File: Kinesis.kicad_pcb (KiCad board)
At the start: 2 copper layers, 122 x 86 mm, 16 parts, among them J1 Right Function, J2 Right Main, J3 Right Thumb, J4 Left Thumb, J5 Left Main, J6 Left Function, U1 proton_c

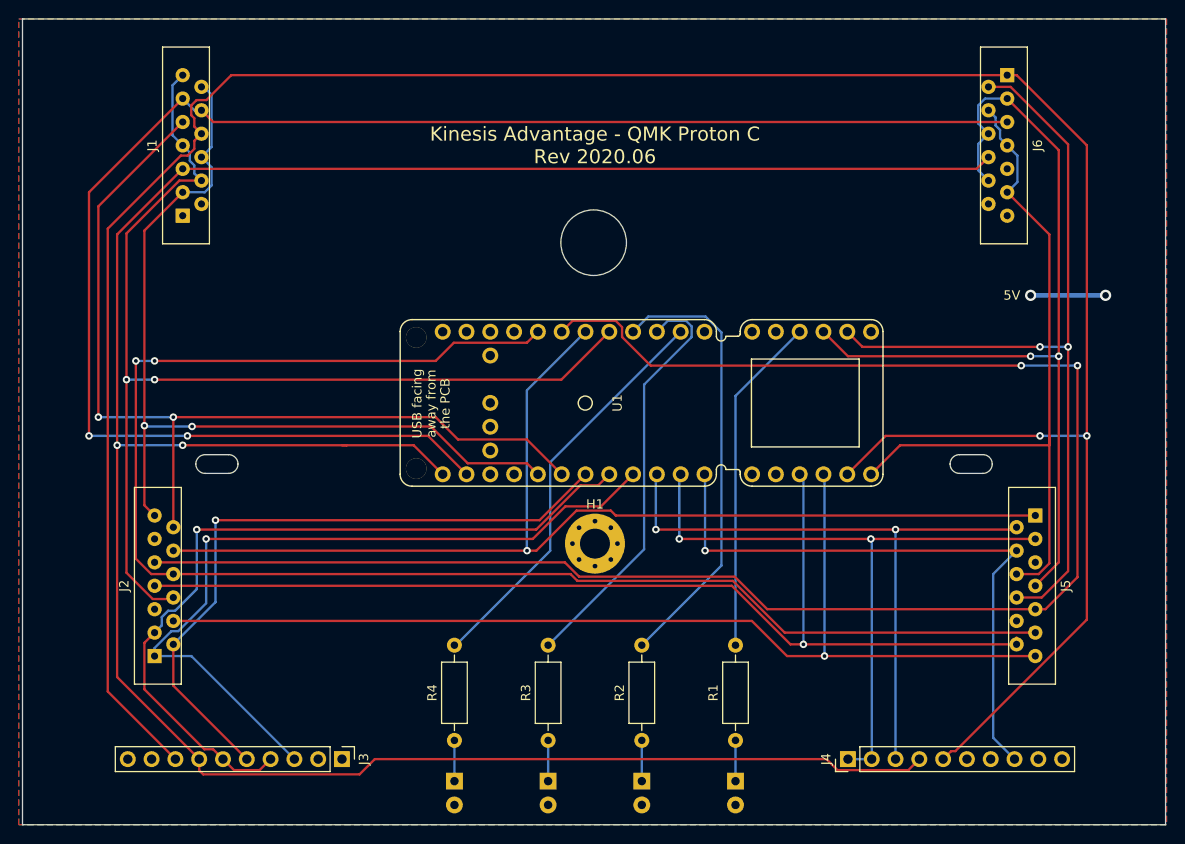
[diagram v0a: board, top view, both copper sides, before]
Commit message: Fix Molex footprints
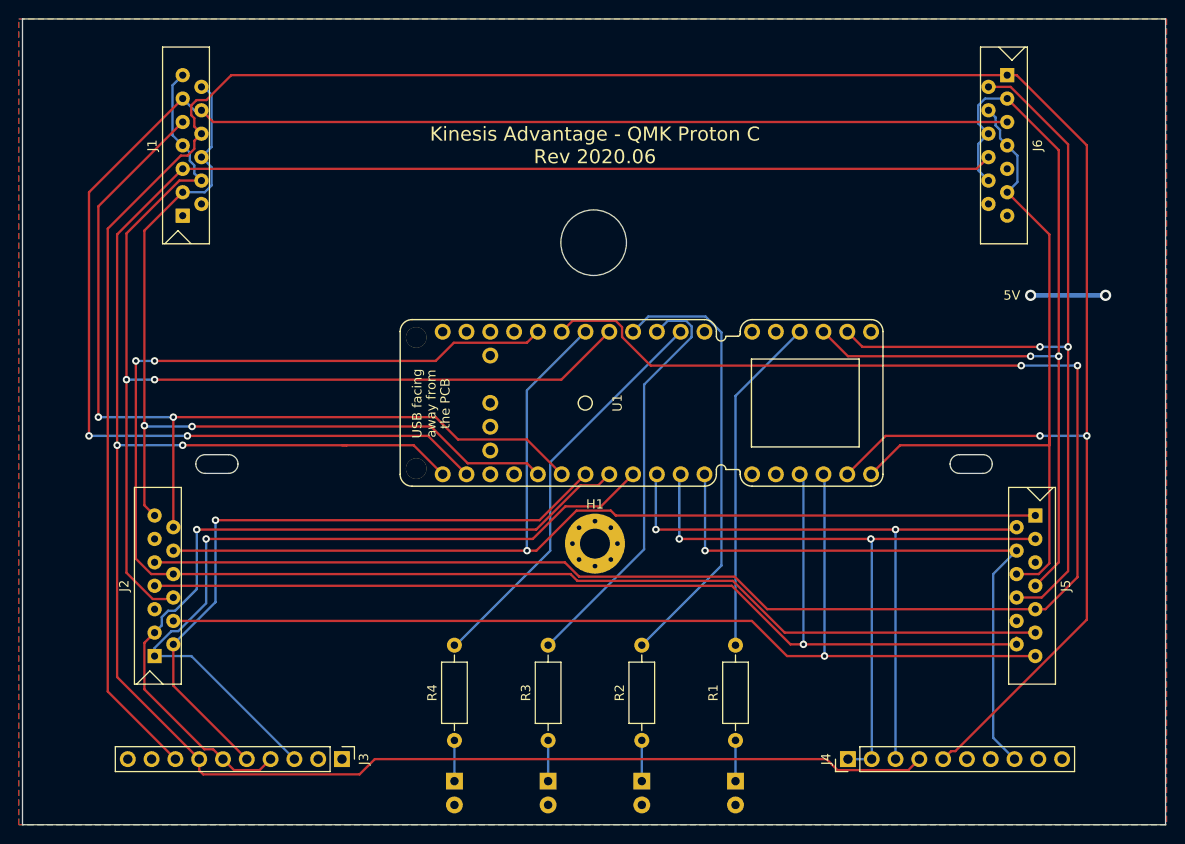
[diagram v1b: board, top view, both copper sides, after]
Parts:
- J1, J2, J5, J6: footprint Connector_FFC-FPC:Molex_FFC-FPC_Easy-On_39-53-2135_13-Contact_Vertical -> Molex_FPC:Molex_FFC-FPC_Easy-On_39-53-2135_13-Contact_Vertical

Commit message: Use TIM4 for LEDs
Also free up debug pins
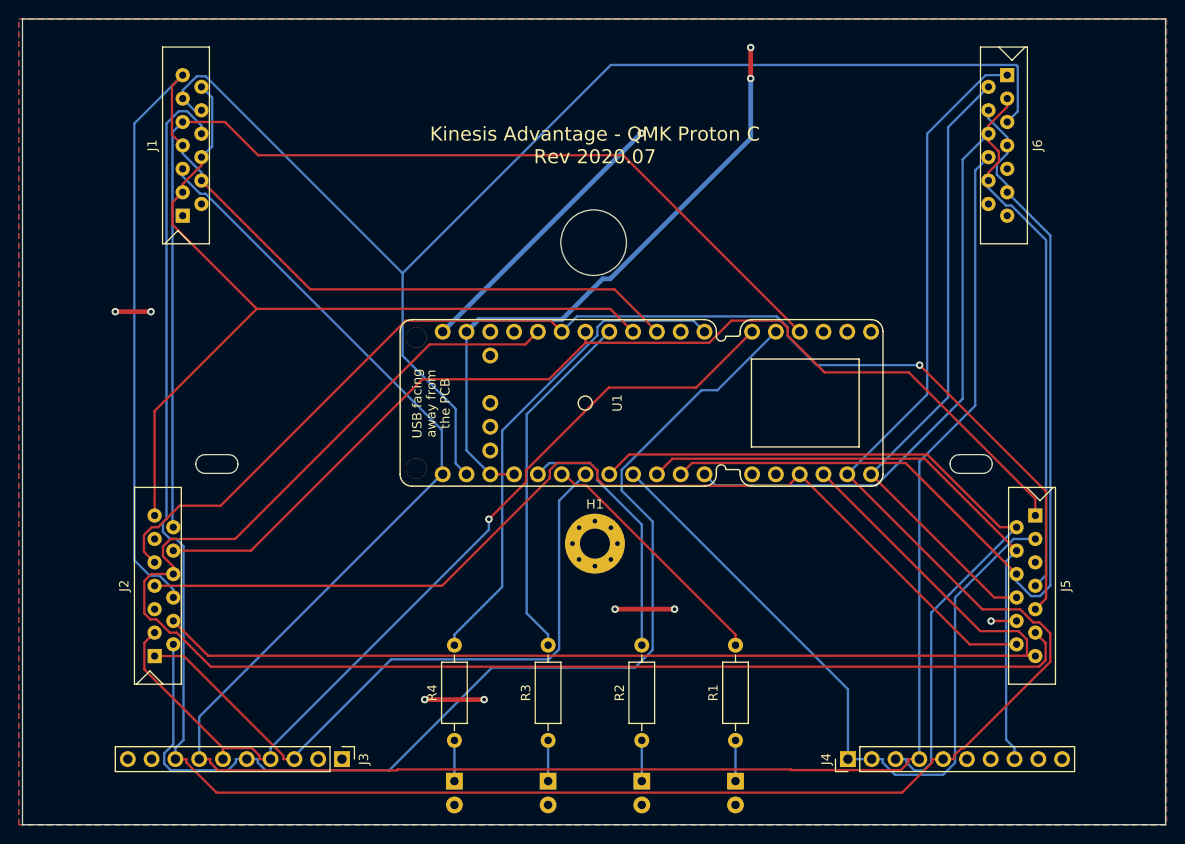
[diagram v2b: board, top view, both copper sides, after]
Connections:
- U1 pad A13: Net-(J5-Pad8) -> (no net)
- U1 pad A14: Net-(J5-Pad7) -> (no net)
- U1 pad A15: Net-(J5-Pad6) -> Net-(J5-Pad8)
- U1 pad B0: Net-(J4-Pad8) -> Net-(J5-Pad7)
- U1 pad B1: Net-(J4-Pad1) -> Net-(J5-Pad6)
- U1 pad B10: (no net) -> Net-(J2-Pad3)
- U1 pad B11: (no net) -> Net-(J2-Pad2)
- U1 pad B12: Net-(R1-Pad2) -> Net-(J1-Pad9)
- U1 pad B13: Net-(R2-Pad2) -> Net-(J1-Pad12)
- U1 pad B14: Net-(R3-Pad2) -> Net-(J1-Pad13)
- U1 pad B15: Net-(R4-Pad2) -> (no net)
- U1 pad B2: Net-(J4-Pad3) -> Net-(J4-Pad8)
- U1 pad B3: Net-(J2-Pad1) -> Net-(J4-Pad1)
- U1 pad B4: Net-(J2-Pad3) -> Net-(J4-Pad3)
- U1 pad B5: Net-(J2-Pad2) -> Net-(J2-Pad1)
- U1 pad B6: Net-(J1-Pad9) -> Net-(R1-Pad2)
- U1 pad B7: Net-(J1-Pad12) -> Net-(R2-Pad2)
- U1 pad B8: Net-(J1-Pad13) -> Net-(R3-Pad2)
- U1 pad B9: (no net) -> Net-(R4-Pad2)
- U1 pad GND: GND -> Net-(U1-PadGND)
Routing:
- net Net-(U1-PadGND): track 0.00 -> 67.4 mm, vias 0 -> 2
- net Net-(J2-Pad9): track 182.7 -> 131.6 mm, vias 2 -> 1
- net Net-(J2-Pad2): track 72.1 -> 115.5 mm, vias 1 -> 0
- net Net-(J1-Pad5): track 272.5 -> 231.3 mm, vias 2 -> 0
- net Net-(J1-Pad10): track 171.2 -> 141.8 mm, vias 2 -> 0
- net Net-(J5-Pad7): track 94.3 -> 118.4 mm, vias 2 -> 0
- net Net-(J5-Pad6): track 77.2 -> 101.2 mm
- net Net-(D1-Pad2): track 8.00 -> 30.0 mm, vias 2 -> 1
- net Net-(J1-Pad9): track 98.7 -> 118.9 mm, vias 2 -> 0
- net Net-(J5-Pad8): track 87.5 -> 67.5 mm, vias 2 -> 0
- net Net-(R2-Pad2): track 47.7 -> 27.8 mm
- net GND: track 0.00 -> 19.2 mm, vias 0 -> 7
- net Net-(J1-Pad8): track 277.2 -> 259.5 mm, vias 2 -> 0
- net Net-(J4-Pad3): track 69.0 -> 81.4 mm, vias 2 -> 0
- net Net-(J2-Pad3): track 83.8 -> 95.6 mm
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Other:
- board text added: "Kinesis Advantage - QMK Proton C Rev 2020.07"
- board text removed: "5V"
- board text removed: "Kinesis Advantage - QMK Proton C Rev 2020.06"
